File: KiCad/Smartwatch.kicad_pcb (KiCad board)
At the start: 2 copper layers, 38.5 x 38.5 mm, 91 parts, among them J1 5358, M1 LCM1027B3605F, Q1 AO3400A, U1 BNO055, U11 MIC5504-1.8YM5, U12 ESP32-S3, U13 BMP280, U14 LD39100PU33R, U2 MIC5504-3.3YM5, U3 MAX30102, U4 MCP9808_DFN, U5 TPS2116DRL, U6 USBLC6-2SC6, U7 BRCL4054DME, U9 GC9A01_IPS_Display_w/_Touch, Y1 40MHz

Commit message: PCB V1
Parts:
- added SW1: SW_Push, Usermade:JXTCONN TS-1010-S26, F.Cu at (154.5, 95.5)
- added SW2: JXTCONN TS-1010-S26, Usermade:JXTCONN TS-1010-S26, F.Cu at (153.3, 87.2)
- added U10: Quectel LC76G, Usermade:quectel lc76g, B.Cu at (129.0, 91.7)
- added Y2: 32.768KHz, Usermade:EPSON Q13FC13500004, B.Cu at (130.2, 108.8)
- added Y3: 32.768KHz, Usermade:EPSON Q13FC13500004, F.Cu at (146.3, 95.3)
- AE2, C17, C18, C19, C2, C21, C23, C24, C25, C29, C3, C30, C33, C34, C35, C36, C38, C4, C5, C7, C8, C9, J1, L2, R11, R12, R13, R19, R20, R22, R24, R25, R26, U1, U14, U2, U4, U7, U9: moved to B.Cu
- moved JP1 77.7 mm to (122.8, 86.9), turned to 165 degrees
- moved AE1 74.6 mm to (121.9, 93.1), turned to -90 degrees
- moved AE2 74.2 mm to (122.6, 98.2), turned to 105 degrees
- moved Y1 67.2 mm to (132.7, 86.4), turned to -60 degrees
- moved M1 66.2 mm to (128.0, 106.0), turned to -135 degrees
- moved U1 65.9 mm to (133.0, 102.0), turned to -45 degrees
- moved U13 65.2 mm to (138.7, 100.5), turned to 45 degrees
- moved R19 62.2 mm to (128.5, 100.9), turned to -165 degrees
- moved R15 61.8 mm to (125.0, 85.7), turned to 75 degrees
- moved R22 61.4 mm to (128.2, 99.9), turned to 15 degrees
- moved R18 60.6 mm to (131.9, 104.8), turned to -45 degrees
- moved R21 58.8 mm to (130.8, 97.7), turned to -45 degrees
- moved C22 57.8 mm to (130.5, 89.5), turned to 105 degrees
- moved L1 57.4 mm to (123.2, 89.8), turned to 180 degrees
- moved U5 57.1 mm to (142.2, 98.6), turned to 135 degrees
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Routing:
- net +3.3V: track 0.00 -> 158.5 mm, vias 0 -> 24
- net GND: track 0.00 -> 73.4 mm, vias 0 -> 12
- net /SCL: track 0.00 -> 36.9 mm, vias 0 -> 2
- net /SDA: track 0.00 -> 35.4 mm, vias 0 -> 4
- net VBAT: track 0.00 -> 33.3 mm, vias 0 -> 4
- net +3.3VGPS: track 0.00 -> 32.3 mm, vias 0 -> 2
- net /CS: track 0.00 -> 25.4 mm, vias 0 -> 1
- net /BAT_REF: track 0.00 -> 25.2 mm, vias 0 -> 5
- net +5V: track 0.00 -> 25.1 mm, vias 0 -> 6
- net /GPSEN: track 0.00 -> 22.6 mm, vias 0 -> 3
- net /LCD_BK: track 0.00 -> 21.2 mm, vias 0 -> 2
- net +1.8V: track 0.00 -> 20.7 mm, vias 0 -> 3
- net /LATCH: track 0.00 -> 20.5 mm, vias 0 -> 2
- net /MOSI: track 0.00 -> 19.7 mm, vias 0 -> 1
- net /GPIO0: track 0.00 -> 18.2 mm, vias 0 -> 2
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- added copper zone on B.Cu, net GND
- added copper zone on F.Cu, net GND
- added copper zone on In1.Cu, net GND
- added copper zone on In2.Cu, net GND
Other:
- copper layers 2 -> 4

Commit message: AAAAAAAAAAAAAAAAA
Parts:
- AE2, C2, C21, C25, C29, C3, C30, C33, C34, C35, C38, C4, C5, C8, C9, J1, L2, R11, R12, R13, R19, R20, U2, U4, U9: moved to F.Cu
- C20, C22, C26, C37, C6, D1, D2, D3, Q1, R10, R14, R15, R17, R18, R21, R23, R27, R28, R29, R5, R8, R9, U11, U13, U5, U6: moved to B.Cu
- moved AE2 32.4 mm to (148.0, 78.0), turned to -30 degrees
- moved C7 30.6 mm to (129.0, 79.5), turned to -90 degrees
- moved BT1 29.9 mm to (122.4, 90.1)
- moved U9 29.9 mm to (130.6, 106.8), turned to 0 degrees
- moved C9 29.4 mm to (127.4, 87.5), turned to 75 degrees
- moved R11 27.9 mm to (129.5, 83.0)
- moved C8 27.7 mm to (128.6, 87.9), turned to 75 degrees
- moved L2 27.5 mm to (145.2, 80.2), turned to -30 degrees
- moved U7 26.9 mm to (123.6, 86.5), turned to 75 degrees
- moved R7 26.5 mm to (129.0, 85.0), turned to 165 degrees
- moved C34 26.1 mm to (145.6, 81.9), turned to -30 degrees
- moved C4 25.8 mm to (123.5, 84.0), turned to 60 degrees
- moved R12 25.8 mm to (130.0, 84.0), turned to 180 degrees
- moved C26 25.7 mm to (130.0, 102.0), turned to 180 degrees
- moved C2 25.6 mm to (123.0, 86.5), turned to -105 degrees
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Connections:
- C19 pad 1: Net-(U1-CAP) -> GND
- C19 pad 2: GND -> Net-(U1-CAP)
- R21 pad 1: GND -> Net-(U1-PS0)
- R21 pad 2: Net-(U1-PS0) -> GND
- R22 pad 1: GND -> Net-(U1-PS1)
- R22 pad 2: Net-(U1-PS1) -> GND
- R24 pad 1: /RX -> Net-(U10-TXD)
- R24 pad 2: Net-(U10-TXD) -> /RX
- U2 pad 1: /BATV -> +3.3VGPS
- U2 pad 3: /GPSEN -> unconnected-(U2-EN-Pad3)
- U2 pad 5: +3.3VGPS -> /BATV
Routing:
- net /LCD_DC: track 7.05 -> 52.8 mm, vias 0 -> 1
- net /LCD_RST: track 10.0 -> 53.9 mm, vias 0 -> 5
- net GND: track 73.4 -> 115.7 mm, vias 12 -> 23
- net /EN: track 9.33 -> 48.4 mm, vias 1 -> 4
- net /TP_INT: track 12.7 -> 49.2 mm, vias 0 -> 1
- net +5V: track 25.1 -> 47.1 mm, vias 6 -> 5
- net VBAT: track 33.3 -> 53.3 mm, vias 4 -> 3
- net /GPSEN: track 22.6 -> 4.05 mm, vias 3 -> 0
- net Net-(U1-~{BOOT_LOAD_PIN}): track 3.04 -> 21.6 mm, vias 0 -> 4
- net +3.3VGPS: track 32.3 -> 15.9 mm
- net /LATCH: track 20.5 -> 4.32 mm, vias 2 -> 1
- net /CS: track 25.4 -> 10.8 mm, vias 1 -> 2
- net Net-(D3-A): track 1.85 -> 14.8 mm, vias 0 -> 4
- net /BATV: track 10.3 -> 22.8 mm, vias 2 -> 4
- net +1.8V: track 20.7 -> 8.18 mm, vias 3 -> 2
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
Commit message: guh
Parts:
- C11, C12, C13, C14, C2, C29, C3, C30, C35, C4, C5, R12, R19, R20, R4, R7, U2, U4, U9, Y1, Y3: moved to B.Cu
- C17, C18, C22, C26, C37, D1, R10, R15, R24, R25, R27, R28, R8, U10, U6, Y2: moved to F.Cu
- moved AE1 33.5 mm to (156.0, 98.0), turned to 75 degrees
- moved L1 26.7 mm to (152.5, 99.3), turned to 75 degrees
- moved AE2 26.5 mm to (122.9, 86.5), turned to 75 degrees
- moved C28 26.2 mm to (152.4, 97.7), turned to 165 degrees
- moved L2 26.2 mm to (121.1, 90.5), turned to 75 degrees
- moved C33 25.4 mm to (121.0, 92.5), turned to -90 degrees
- moved C34 25.0 mm to (122.1, 90.5), turned to -105 degrees
- moved R11 25.0 mm to (154.4, 85.6), turned to 15 degrees
- moved R12 24.4 mm to (154.4, 85.7), turned to -165 degrees
- moved C27 24.2 mm to (151.2, 100.0), turned to -105 degrees
- moved C20 24.2 mm to (154.7, 91.9), turned to 0 degrees
- moved R1 23.2 mm to (143.0, 77.3), turned to 135 degrees
- moved M1 23.1 mm to (138.3, 77.6), turned to 135 degrees
- moved J1 22.9 mm to (130.9, 85.2), turned to 135 degrees
- moved C35 22.5 mm to (126.5, 98.0), turned to -90 degrees
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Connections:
- R24 pad 1: Net-(U10-TXD) -> /RX
- R24 pad 2: /RX -> Net-(U10-TXD)
- U2 pad 1: +3.3VGPS -> /BATV
- U2 pad 3: unconnected-(U2-EN-Pad3) -> /GPSEN
- U2 pad 5: /BATV -> +3.3VGPS
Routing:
- net /CS: track 10.8 -> 75.6 mm
- net /MOSI: track 11.2 -> 66.8 mm, vias 1 -> 2
- net /LCD_DC: track 52.8 -> 13.9 mm
- net /SCLK: track 19.5 -> 57.4 mm, vias 2 -> 6
- net /LCD_RST: track 53.9 -> 16.4 mm, vias 5 -> 1
- net /MISO: track 18.9 -> 55.9 mm, vias 1 -> 8
- net GND: track 115.7 -> 86.5 mm, vias 23 -> 25
- net VBAT: track 53.3 -> 24.8 mm
- net /TP_INT: track 49.2 -> 21.2 mm
- net /LCD_BK: track 14.1 -> 38.9 mm, vias 1 -> 4
- net +5V: track 47.1 -> 23.3 mm, vias 5 -> 3
- net /VIBE: track 5.17 -> 27.6 mm, vias 0 -> 4
- net /BATV: track 22.8 -> 43.1 mm, vias 4 -> 3
- net Net-(U1-~{BOOT_LOAD_PIN}): track 21.6 -> 1.60 mm, vias 4 -> 0
- net /CHRG_ST: track 17.7 -> 35.0 mm, vias 1 -> 5
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
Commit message: V5
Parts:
- BT1, C1, C10, C17, C18, C21, C22, C31, C32, C8, C9, D1, JP1, R10, R11, R13, R6, Y2: moved to B.Cu
- C2, C4, C7, R14, R29, R4, R5, U13, U14, U4, U5, Y3: moved to F.Cu
- moved SW1 32.3 mm to (124.9, 100.1), turned to 110 degrees
- moved C26 31.4 mm to (149.0, 81.0), turned to 0 degrees
- moved AE2 31.2 mm to (143.5, 110.0), turned to 15 degrees
- moved R5 31.2 mm to (124.0, 96.1), turned to -165 degrees
- moved U9 30.7 mm to (148.6, 78.7), turned to 180 degrees
- moved R6 30.7 mm to (123.2, 95.2), turned to 15 degrees
- moved C1 30.4 mm to (123.5, 94.0), turned to -165 degrees
- moved M1 28.2 mm to (149.5, 103.5), turned to 180 degrees
- moved R12 27.8 mm to (127.0, 90.4), turned to 0 degrees
- moved D2 27.7 mm to (126.0, 94.0), turned to 105 degrees
- moved R11 27.6 mm to (127.0, 89.3), turned to 180 degrees
- moved D3 26.9 mm to (126.0, 98.3), turned to 15 degrees
- moved C34 26.8 mm to (140.0, 110.5), turned to 90 degrees
- moved L2 26.8 mm to (139.0, 110.5), turned to -90 degrees
- moved R7 26.5 mm to (126.0, 96.5)
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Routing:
- net /SCL: track 27.8 -> 76.2 mm, vias 3 -> 5
- net /CS: track 75.6 -> 30.1 mm, vias 2 -> 1
- net GND: track 86.5 -> 130.1 mm, vias 25 -> 17
- net /MOSI: track 66.8 -> 27.6 mm, vias 2 -> 1
- net /MISO: track 55.9 -> 18.8 mm, vias 8 -> 1
- net /SCLK: track 57.4 -> 25.1 mm, vias 6 -> 0
- net /BT_2: track 14.0 -> 43.6 mm, vias 2 -> 1
- net /SDA: track 35.1 -> 64.0 mm, vias 7 -> 5
- net /EN: track 33.1 -> 8.07 mm, vias 2 -> 1
- net /BT_1: track 19.8 -> 39.0 mm, vias 2 -> 6
- net /VIBE: track 27.6 -> 10.4 mm, vias 4 -> 2
- net /BATV: track 43.1 -> 28.2 mm
- net /LCD_BK: track 38.9 -> 24.1 mm, vias 4 -> 2
- net /LATCH: track 14.1 -> 26.1 mm, vias 0 -> 2
- net Net-(U10-D_SEL): track 0.00 -> 11.9 mm, vias 1 -> 2
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
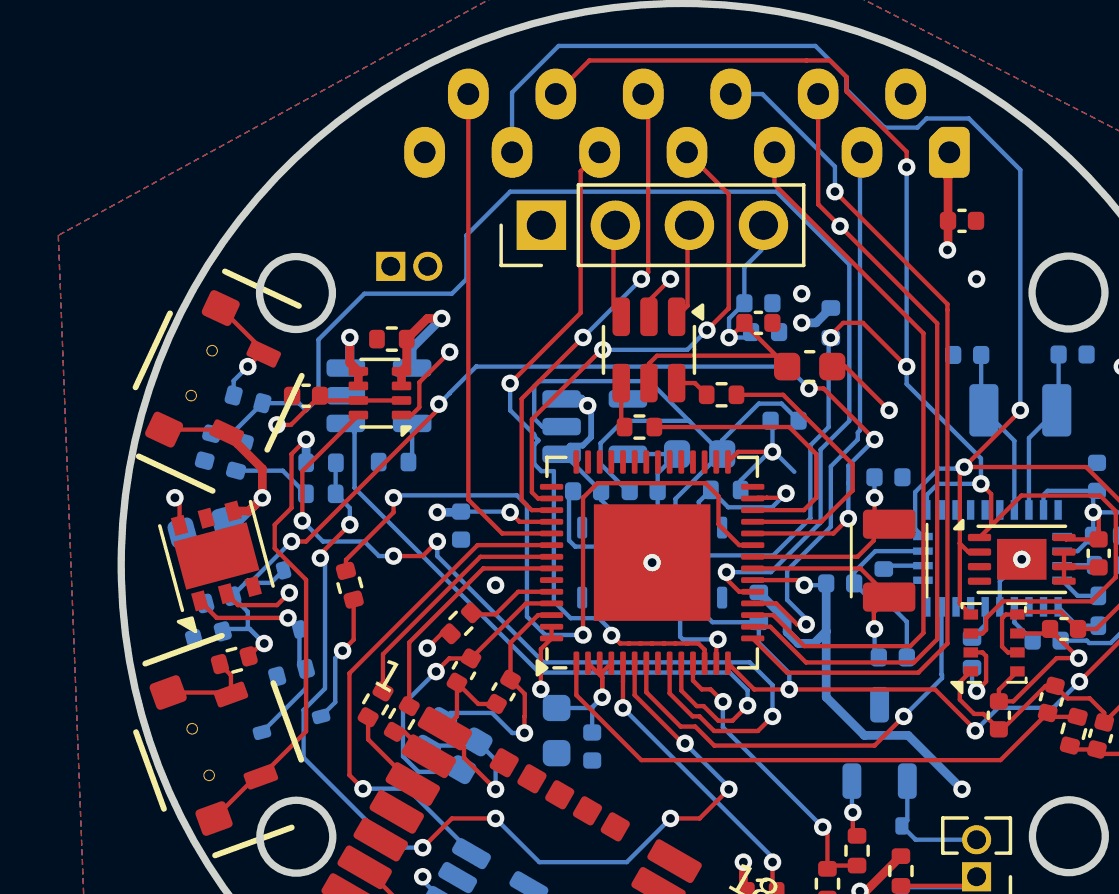
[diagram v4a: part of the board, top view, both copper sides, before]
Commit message: added teardrops, cleaned up a few traces
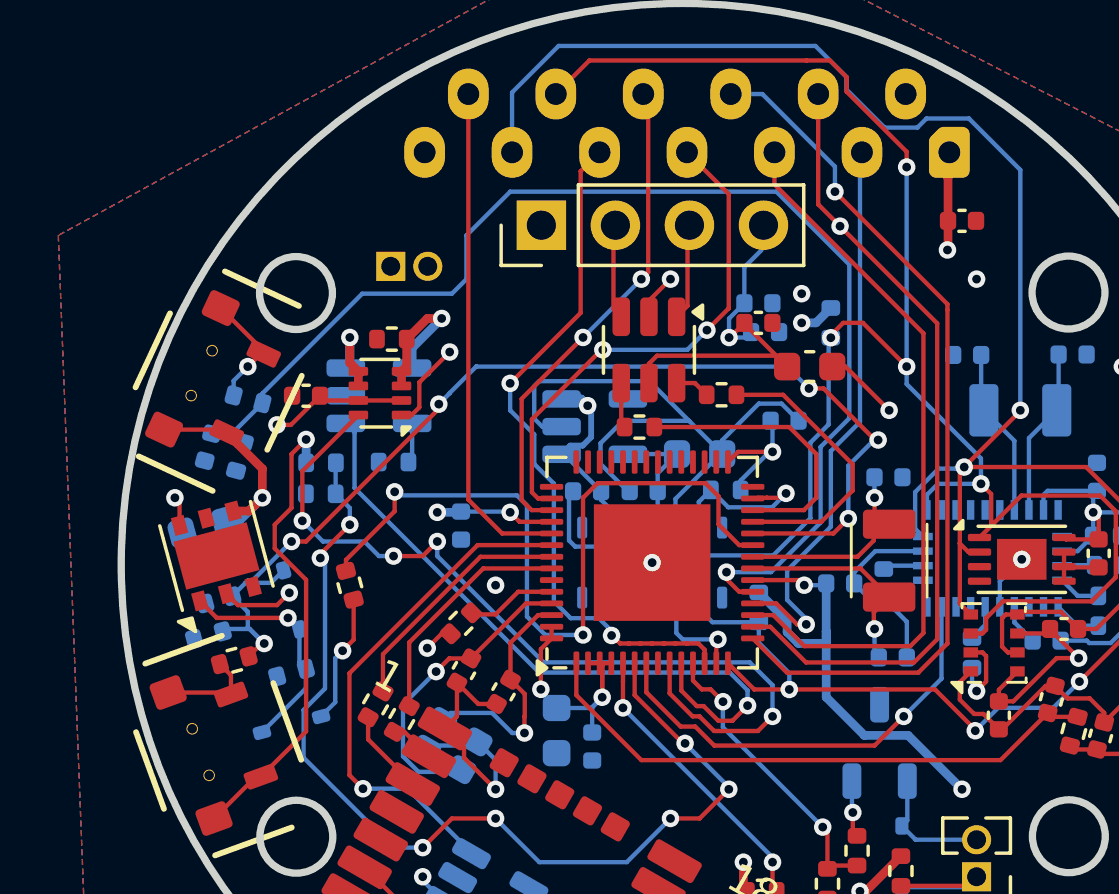
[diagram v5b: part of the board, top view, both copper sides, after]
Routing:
- net GND: track 130.1 -> 127.4 mm
- net /BT_2: track 43.6 -> 42.4 mm

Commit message: gonna jump off a builing on facebook live
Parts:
- added R16: 10k, Resistor_SMD:R_0402_1005Metric, B.Cu at (133.0, 103.5)
- Y1: moved to F.Cu
- moved R14 13.4 mm to (126.9, 105.0), turned to -105 degrees
- moved AE2 5.59 mm to (148.5, 107.5), turned to 30 degrees
- moved C34 4.60 mm to (144.5, 109.5), turned to 105 degrees
- moved L2 4.58 mm to (143.5, 109.8), turned to -75 degrees
- moved C33 4.58 mm to (142.6, 110.0), turned to -75 degrees
- moved C36 4.42 mm to (136.8, 108.4), turned to -105 degrees
- moved C29 4.35 mm to (134.5, 107.5), turned to 75 degrees
- moved C30 4.33 mm to (135.9, 108.1), turned to 75 degrees
- moved C35 4.07 mm to (132.8, 107.0), turned to -105 degrees
- moved U2 3.34 mm to (136.0, 104.3), turned to -15 degrees
- moved C16 1.92 mm to (135.0, 98.0), turned to -15 degrees
- moved U10 1.82 mm to (137.0, 103.3), turned to -15 degrees
- moved C15 1.78 mm to (130.5, 97.5), turned to -105 degrees
- moved Y1 1.65 mm to (132.5, 97.7), turned to -15 degrees
- moved J1 1.50 mm to (136.1, 81.2)
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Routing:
- net GND: track 127.4 -> 137.8 mm
- net Net-(U10-RXD): track 2.93 -> 7.28 mm
- net /LCD_DC: track 17.5 -> 21.9 mm, vias 2 -> 3
- net /XTALN: track 10.6 -> 7.06 mm, vias 1 -> 0
- net /BATV: track 28.2 -> 30.9 mm
- net /XTALP: track 8.33 -> 5.62 mm, vias 1 -> 0
- net /GPSEN: track 17.6 -> 20.2 mm
- net Net-(U10-TXD): track 1.53 -> 4.13 mm
- net /SCLK: track 25.1 -> 27.3 mm
- net Net-(R5-Pad2): track 3.38 -> 1.30 mm
- net Net-(R9-Pad2): track 4.02 -> 1.94 mm
- net VBAT: track 26.1 -> 24.1 mm
- net Net-(U10-D_SEL): track 11.9 -> 9.86 mm
- net +3.3V: track 162.2 -> 164.1 mm
- net /LCD_RST: track 17.0 -> 18.9 mm
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
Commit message: cenetered charging pins?
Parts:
- moved J1 0.25 mm to (135.8, 81.1)
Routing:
- net GND: track 137.8 -> 136.9 mm
- net /SCLK: track 27.3 -> 28.2 mm
